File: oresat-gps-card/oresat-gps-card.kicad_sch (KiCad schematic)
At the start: 16 parts, among them J1 J-SAMTEC-TFM-120-01-L-D-RA, J3 GRPB041VWVN-RC, J6 SM14B-SHLS-TF

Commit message: Routine Push
Schematic finished. Components laid out, chasing ERCs.
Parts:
- removed TP140, TP141: 0.03x0.04, oresat-misc:TestPoint_Pad_D1.0mm, symbol oresat-misc:Test-Point-1mm-round
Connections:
- net CAN1_H: no longer names the net of J1.33
- net CAN1_H: no longer J1.34
- net CAN1_L: no longer names the net of J1.35
- net CAN1_L: no longer J1.36
- no-connect marks 18 -> 22
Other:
- sheet MAX2769 ports: added MAX-LD; removed none
- moved on the sheet: CM1, J1, J3, J6, R68, TP159

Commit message: Routine Push
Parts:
- removed FID5, FID6: Fiducial, Fiducial:Fiducial_1mm_Mask2mm, symbol Mechanical:Fiducial
- TP159: footprint oresat-misc:TestPoint_Pad_D1.0mm -> oresat-misc:TestPoint-0.75mm-th
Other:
- moved on the sheet: CM1, J1, J3, J6, R68, TP159

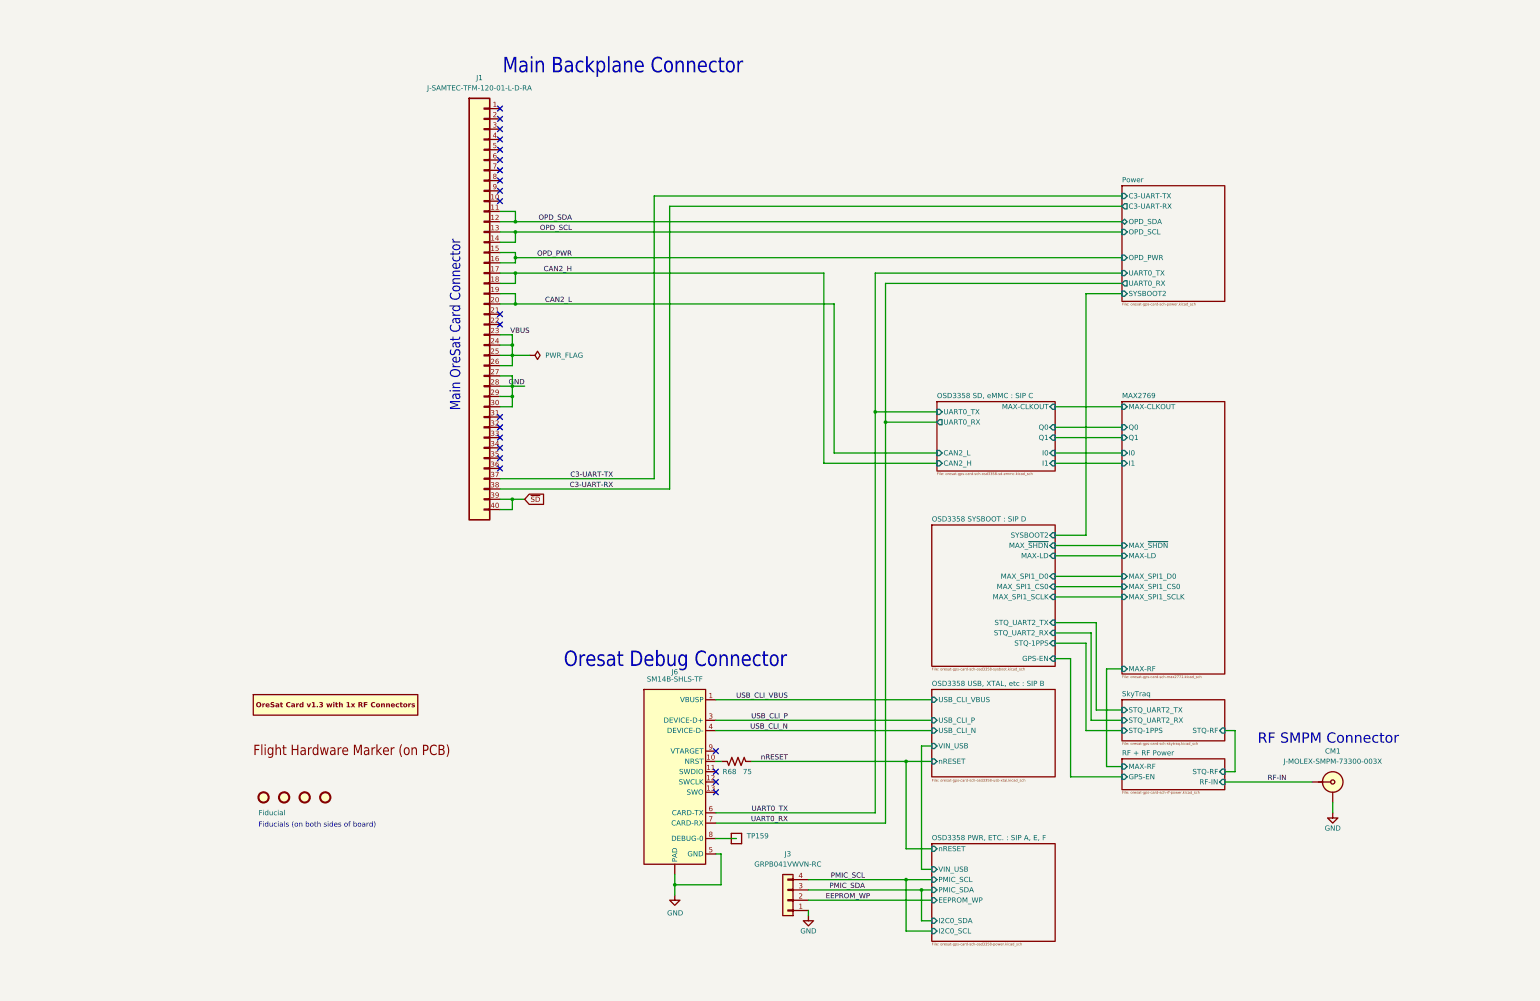
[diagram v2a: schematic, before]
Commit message: General cleanup of schematic and layout
Updated .gitignore, updates DRU file, moved RF lines to RF-50-MIN (max is just too big),
lots of cleanup on the root page to make it pretty, cleaned up some redudant labels,
updated SMPM connector and added rule zone, updated PCB outline to include NPTH drills
for SMPM connectors, began cleanup of OPD.
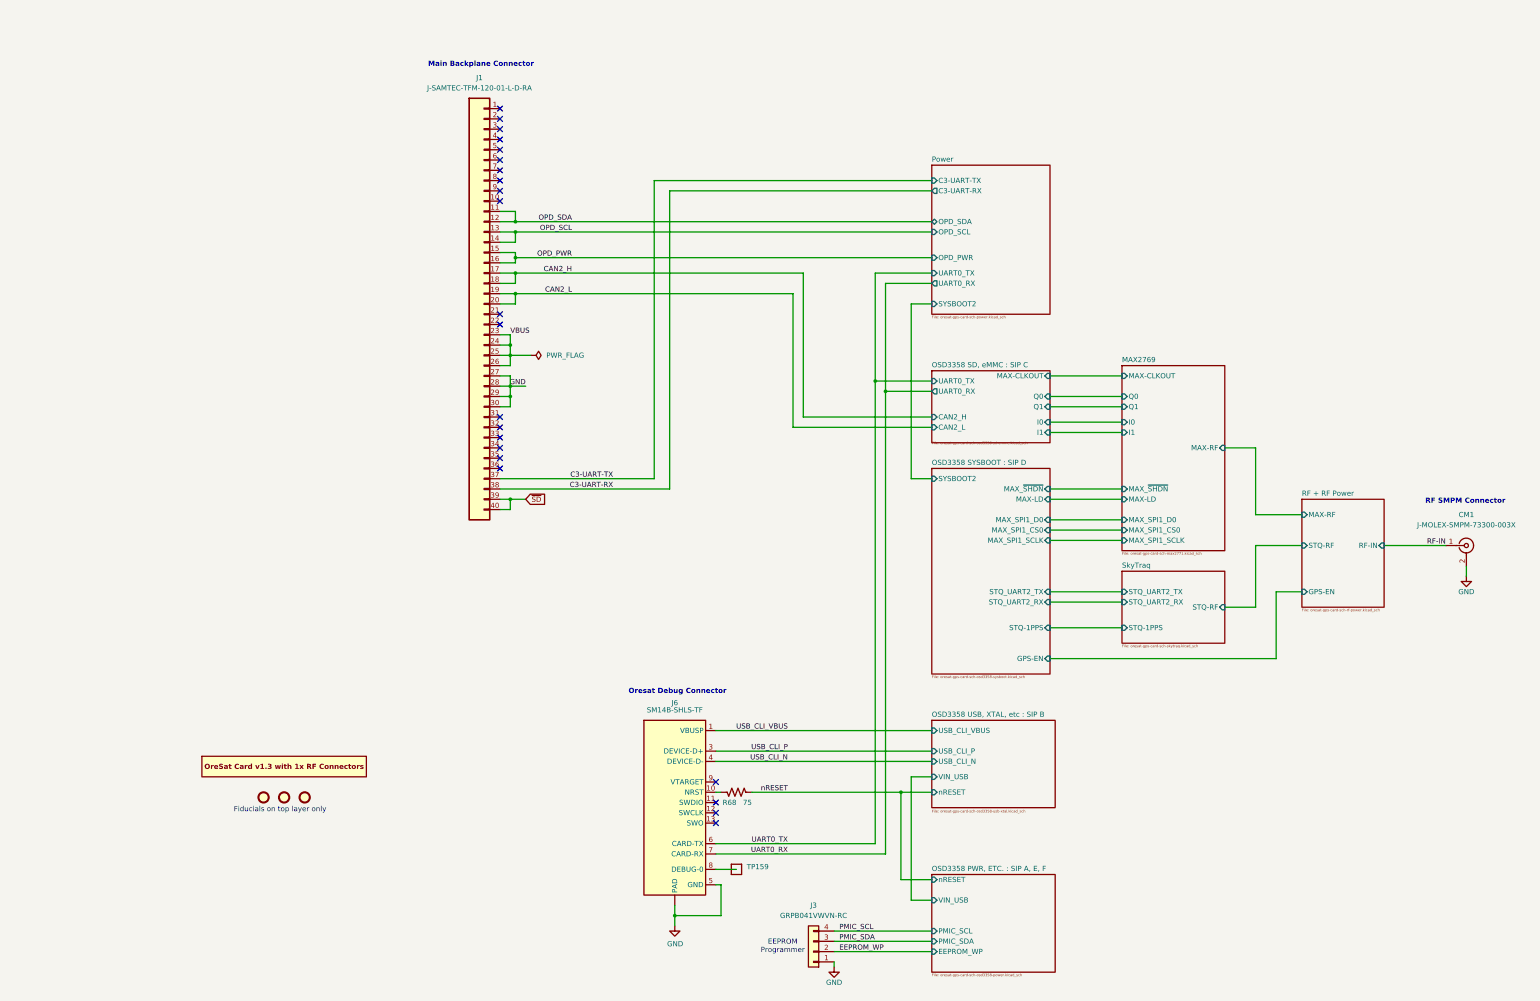
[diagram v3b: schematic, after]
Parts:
- removed FID4: Fiducial, Fiducial:Fiducial_1mm_Mask2mm, symbol Mechanical:Fiducial
- removed FLIGHT1: FLIGHTMARKER, oresat-graphics:FLIGHTMARKER, symbol oresat-graphics:FLIGHTMARKER
- CM1: symbol oresat-connectors:J-MOLEX-SMPM-73300-002X -> Connector:Conn_Coaxial
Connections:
- net GND: now also CM1.2 (Ext); no longer CM1.SHLD
- net RF-IN: now also CM1.1 (In); no longer CM1.SIG
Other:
- sheet OSD3358 PWR, ETC. : SIP A, E, F ports: added none; removed I2C0_SCL, I2C0_SDA
- note added: "EEPROM Programmer"
- note added: "Fiducials on top layer only"
- note removed: "Fiducials (on both sides of board)"
- note removed: "Main OreSat Card Connector"
- moved on the sheet: J3, J6, R68, TP159
